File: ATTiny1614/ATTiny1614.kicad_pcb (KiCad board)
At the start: 2 copper layers, 18 x 29.3 mm, 29 parts, among them J1 Conn_01x07, J2 Conn_01x02, J3 Conn_01x07, J4 ISP6, U1 AP2204K-ADJ

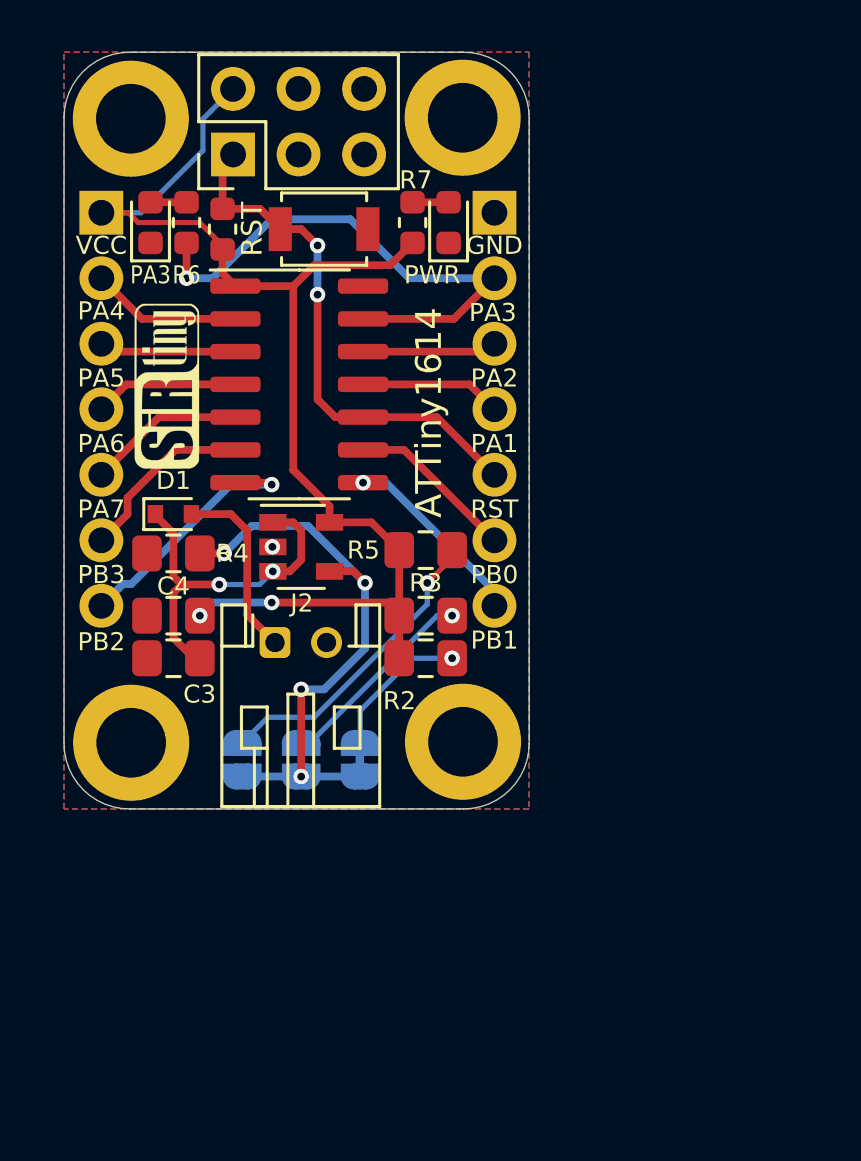
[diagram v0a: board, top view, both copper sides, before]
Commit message: Spacings Updated
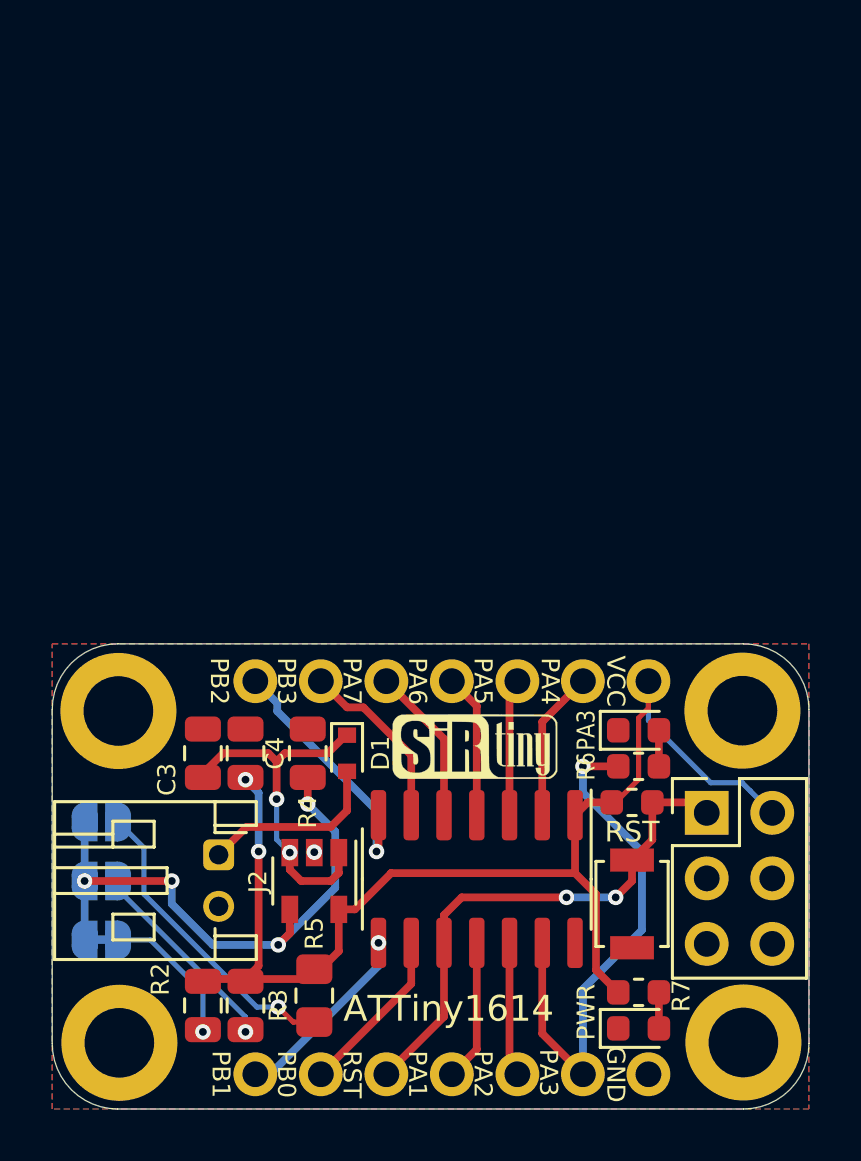
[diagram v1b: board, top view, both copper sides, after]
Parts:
- C3, C4: footprint Capacitor_SMD:C_0805_2012Metric_Pad1.15x1.40mm_HandSolder -> Capacitor_SMD:C_0805_2012Metric
- J1, J3: moved to F.Cu
- R2, R3, R4: footprint Resistor_SMD:R_0805_2012Metric_Pad1.15x1.40mm_HandSolder -> Resistor_SMD:R_0805_2012Metric
- moved REF** 37.5 mm to (127.8, 113.4), turned to 270 degrees
- moved J3 33.9 mm to (124.1, 114.7), turned to 270 degrees
- moved REF** 33.0 mm to (127.7, 100.6), turned to 270 degrees
- moved PWR 32.1 mm to (123.7, 112.9), turned to 0 degrees
- moved J4 31.4 mm to (126.3, 104.5), turned to 0 degrees
- moved R7 31.1 mm to (123.7, 111.5), turned to 0 degrees
- moved RST 28.8 mm to (123.4, 108.1), turned to 270 degrees
- moved J1 27.9 mm to (124.1, 99.4), turned to 270 degrees
- moved R6 27.4 mm to (123.7, 102.7), turned to 0 degrees
- moved R1 27.3 mm to (123.4, 104.1), turned to 180 degrees
- moved PA3 27.3 mm to (123.7, 101.3), turned to 0 degrees
- moved ATTiny1614 20.4 mm to (117.4, 107.1), turned to 270 degrees
- moved G*** 19.7 mm to (118.1, 103.5), turned to 90 degrees
- moved G*** 18.4 mm to (117.3, 102.0), turned to 0 degrees
- moved R5 17.8 mm to (111.1, 111.6), turned to 270 degrees
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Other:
- board size 18 x 29.3 mm -> 29.3 x 18 mm

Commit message: Silkscreens Orientated
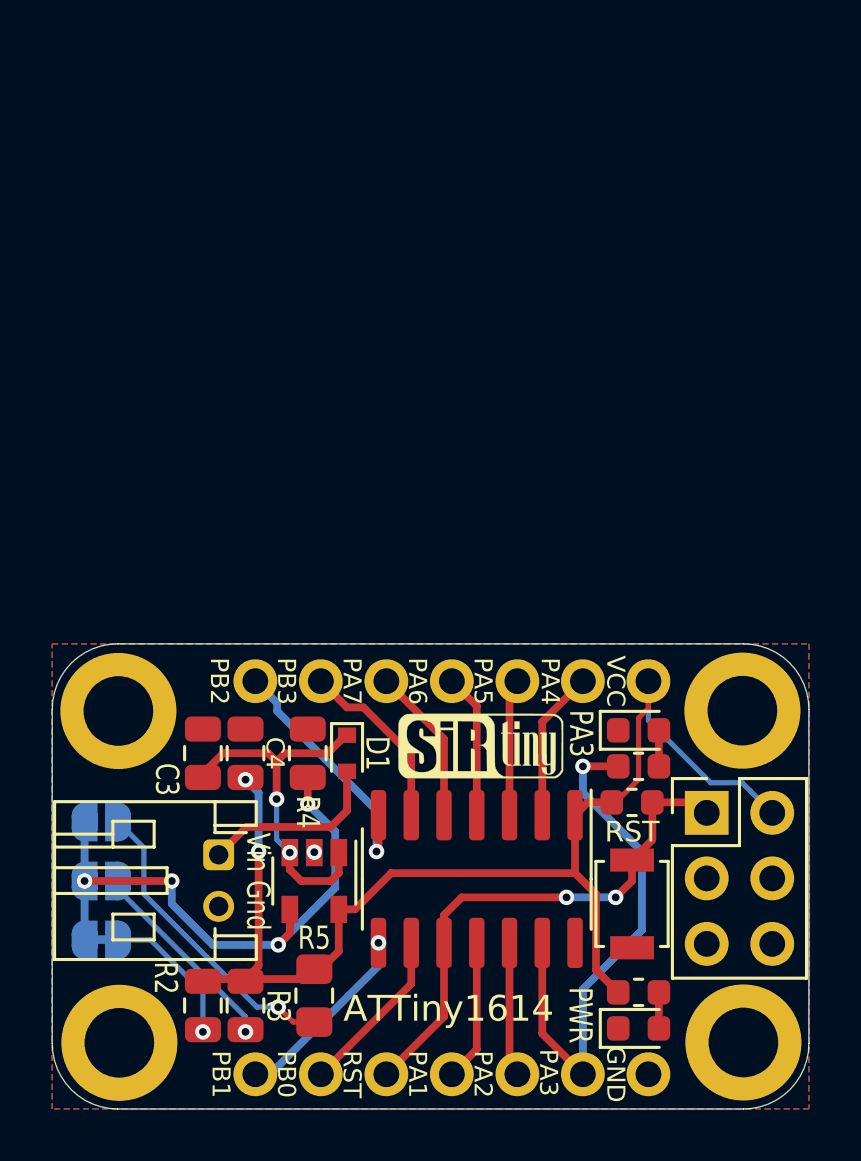
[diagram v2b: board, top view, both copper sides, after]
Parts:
- J1, J3: moved to B.Cu
- Vin Gnd: renamed from J2
- moved G*** 0.23 mm to (117.6, 102.0)
- turned J1 to 90 degrees
- turned J3 to 90 degrees
